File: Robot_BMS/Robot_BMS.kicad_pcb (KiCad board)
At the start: 4 copper layers, 108.6 x 103.7 mm, 117 parts, among them IC1 AP33772DKZ-13, IC1 STUSB4710AQTR, IC2 BQ76922RSNR, J1 632723300011, J2 39-30-0040, J3 Qwiik1, J4 Qwiik1, J5 Qwiik1, J6 Qwiik1, J7 694108301002, J8 691137710002, Q1 2N7002, Q2 NDT3055L, Q3 NDT3055L, Q4 SIS413DN-T1-GE3, Q5 2N7002, Q6 SIS413DN-T1-GE3, U1 TPS54308DDCR, U2 LM3488MM, U3 CSD18563Q5A

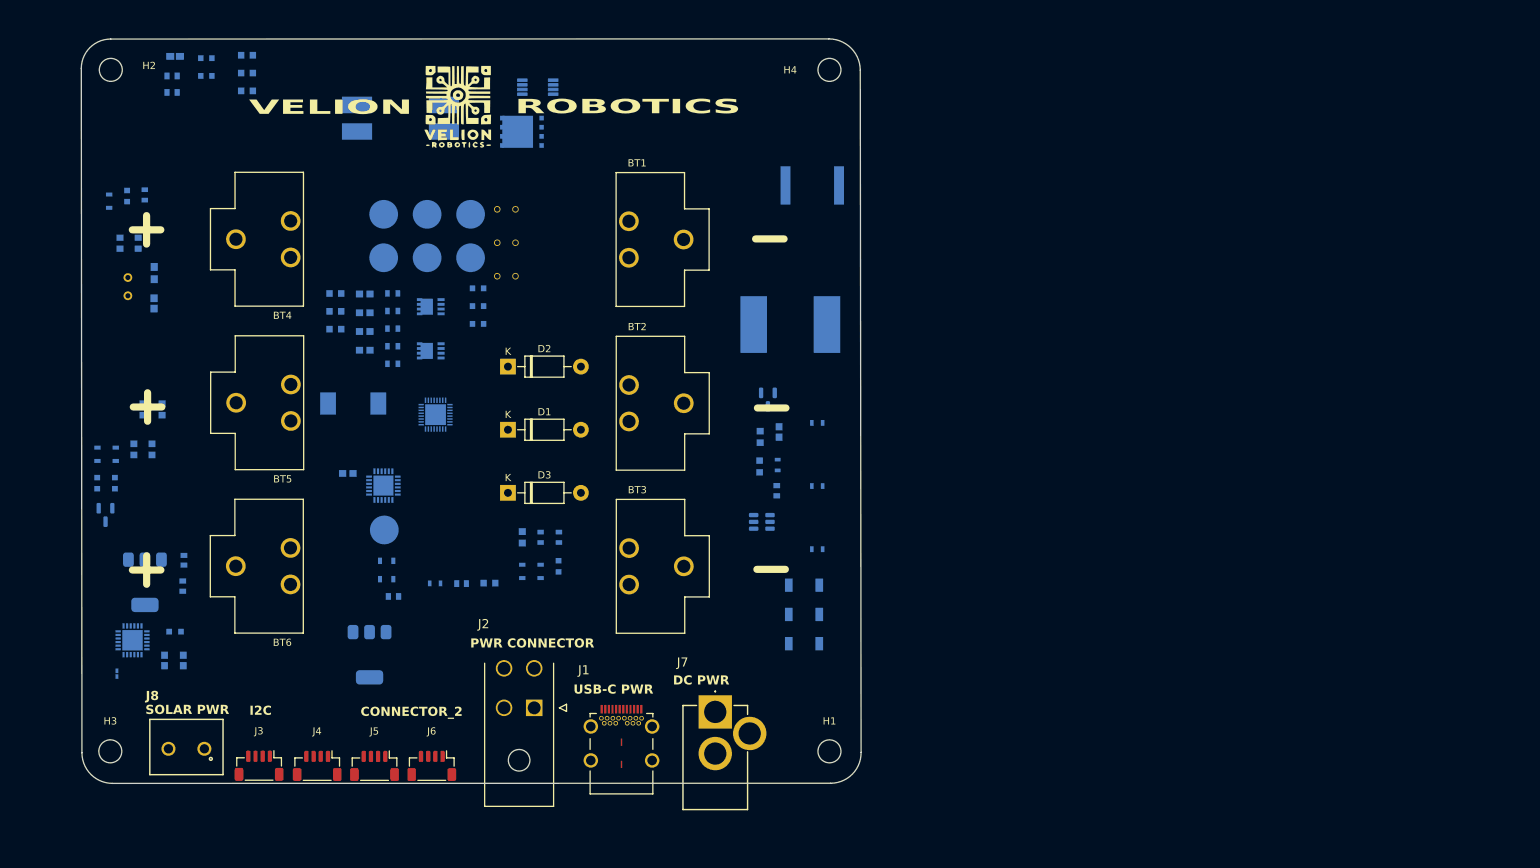
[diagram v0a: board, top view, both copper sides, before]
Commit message: PCB layout up to charging circuit
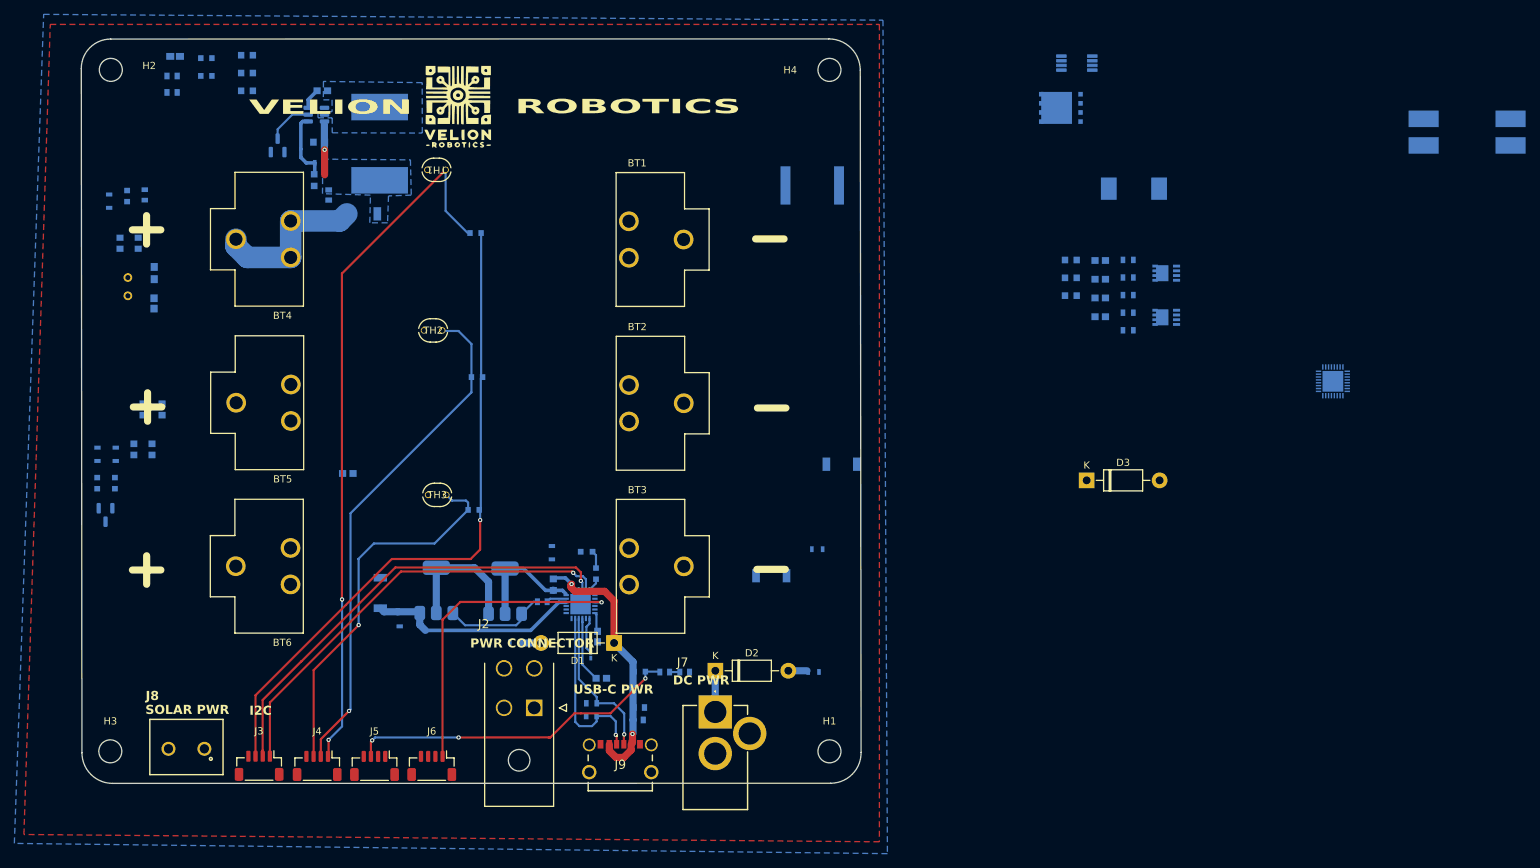
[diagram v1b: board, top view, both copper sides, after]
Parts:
- removed the C4 at (108.8, 91.3)
- removed the C5 at (108.8, 93.9)
- removed the IC1 at (108.4, 80.8)
- removed J1: 632723300011, RobotBMS:632723300011
- removed R12: 100, RobotBMS:RESC1608X55N
- removed the R6 at (115.6, 94.5)
- removed TP1, TP2: NTC1, TestPoint:TestPoint_Pad_D4.0mm
- removed TP3, TP4: NTC2, TestPoint:TestPoint_Pad_D4.0mm
- removed TP5, TP6: NTC3, TestPoint:TestPoint_Pad_D4.0mm
- removed TP7: VBUS_Test, TestPoint:TestPoint_Pad_D4.0mm
- added CR4: CMS05TE12L_Q_M, RobotBMS:M-FLAT_TOS, B.Cu at (105.4, 43.0)
- added J9: UJC-H-G-SMT-P6-TR, RobotBMS:UJCHGSMT2P6TR, F.Cu at (141.3, 119.9)
- added R35: 10k, RobotBMS:RC0603N_YAG, B.Cu at (144.1, 106.8)
- added R36: 1k, RobotBMS:RES_V0603_VIS, B.Cu at (150.3, 106.8)
- TH1, TH2, TH3: moved to F.Cu
- moved L2 148.5 mm to (259.3, 31.6)
- moved IC2 125.0 mm to (240.6, 66.3)
- moved D4 112.8 mm to (212.9, 39.5)
- moved R19 102.5 mm to (204.1, 49.4)
- moved R21 102.5 mm to (204.1, 51.9)
- moved R24 102.5 mm to (204.1, 54.4)
- moved C12 102.5 mm to (208.2, 49.5)
- moved C13 102.5 mm to (208.2, 52.1)
- moved C14 102.5 mm to (208.2, 54.7)
- moved C16 102.5 mm to (208.2, 57.3)
- moved Q4 102.5 mm to (217.3, 51.3)
- moved Q6 102.5 mm to (217.3, 57.4)
- moved R14 102.5 mm to (212.1, 49.4)
- moved R15 102.5 mm to (212.1, 51.9)
- moved R16 102.5 mm to (212.1, 54.3)
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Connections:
- C3 pad 2: BATT+ -> Net-(C3-Pad2)
- J5 pad 3: GND -> /To MCU OR System/MCU_USB_DETECT
- L1 pad 2: BATT+ -> Net-(C3-Pad2)
- R11 pad 1: VBUS -> /To MCU OR System/MCU_USB_DETECT
- R11 pad 2: GND -> Net-(R11-Pad2)
- R4 pad 2: BATT+ -> Net-(C3-Pad2)
- TH1 pad 1: unconnected-(TH1-Pad1) -> /Thermistors/ADC1_MCU
- TH1 pad 2: unconnected-(TH1-Pad2) -> GND
- TH2 pad 1: unconnected-(TH2-Pad1) -> GND
- TH2 pad 2: unconnected-(TH2-Pad2) -> /Thermistors/ADC2_MCU
- TH3 pad 1: unconnected-(TH3-Pad1) -> GND
- TH3 pad 2: unconnected-(TH3-Pad2) -> /Thermistors/ADC3_MCU
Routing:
- net /Thermistors/ADC1_MCU: track 0.00 -> 98.5 mm, vias 0 -> 2
- net 3V3: track 0.00 -> 92.6 mm, vias 0 -> 1
- net /Thermistors/ADC2_MCU: track 0.00 -> 70.9 mm, vias 0 -> 1
- net /Battery Management/SDA: track 0.00 -> 62.6 mm, vias 0 -> 1
- net /Battery Management/SCL: track 0.00 -> 60.9 mm, vias 0 -> 1
- net /Thermistors/ADC3_MCU: track 0.00 -> 52.7 mm, vias 0 -> 1
- net /To MCU OR System/MCU_USB_DETECT: track 0.00 -> 47.1 mm, vias 0 -> 3
- net /To MCU OR System/USB_C_Interrupt: track 0.00 -> 43.2 mm, vias 0 -> 1
- net VBUS: track 0.00 -> 38.3 mm, vias 0 -> 2
- net /Charging Circuit/USB_C: track 0.00 -> 30.2 mm
- net /USB-C/CC1: track 0.00 -> 25.0 mm, vias 0 -> 1
- net BATT+: track 0.00 -> 22.6 mm
- net /USB-C/CC2: track 0.00 -> 21.6 mm, vias 0 -> 1
- net Net-(Q2-S): track 0.00 -> 18.8 mm
- net /USB-C/VCC: track 0.00 -> 16.3 mm
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- added copper zone on B.Cu, net GND
- added copper zone on F.Cu, net GND
- added copper zone on B.Cu, net Net-(C3-Pad2)
- added copper zone on B.Cu, net Net-(U1-SW)
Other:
- copper layers 4 -> 2
- board text removed: "CONNECTOR_2"

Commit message: halfway throgh battery management pcb layout
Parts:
- NTC1: renamed from RT1; value 10k -> 10000
- moved C20 170.6 mm to (246.0, 73.9)
- moved C22 170.6 mm to (242.4, 71.6)
- moved C25 170.6 mm to (239.8, 59.7)
- moved R30 170.6 mm to (241.3, 65.5)
- moved R33 170.6 mm to (243.8, 65.5)
- moved R35 170.6 mm to (242.3, 59.0)
- moved C23 170.6 mm to (246.1, 69.7)
- moved R29 170.6 mm to (244.7, 58.8)
- moved C21 144.6 mm to (243.8, 113.9)
- moved C24 123.3 mm to (193.4, 68.1)
- moved C26 123.3 mm to (193.0, 70.8)
- moved C27 123.3 mm to (193.0, 73.1)
- moved R31 123.3 mm to (203.4, 67.9)
- moved R32 123.3 mm to (203.4, 70.4)
- moved R34 123.3 mm to (203.4, 72.9)
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- renumbered CR4 to CR1, CR1 to CR2, CR2 to CR3, CR3 to CR4, J9 to J1, J2 to J3, J3 to J4, J4 to J5, J5 to J6, J6 to J7, J7 to J8, J8 to J9, R35 to R11, R11 to R12, R36 to R13, R13 to R14, R14 to R15, R15 to R16, R16 to R17, R17 to R18, R18 to R19, R19 to R20, R20 to R21, R21 to R22, R22 to R23, R23 to R24, R24 to R25, R25 to R26, R26 to R27, R27 to R28, R28 to R29, R29 to R30, R30 to R31, R31 to R32, R32 to R33, R33 to R34, R34 to R35
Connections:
- CR1 pad 2: BATT+ -> /Charging Circuit/TO_LOAD
- J3 pad 1: GND -> /Battery Management/TO_LOAD_GND
- J3 pad 2: GND -> /Battery Management/TO_LOAD_GND
- Q4 pad 10: (no net) -> BATT+
- Q4 pad 11: (no net) -> BATT+
- Q4 pad 9: (no net) -> BATT+
- Q6 pad 10: (no net) -> Net-(Q4-S_1)
- Q6 pad 11: (no net) -> Net-(Q4-S_1)
- Q6 pad 9: (no net) -> Net-(Q4-S_1)
- R21 pad 1: GND -> /Battery Management/TO_LOAD_GND
- R22 pad 1: GND -> /Battery Management/TO_LOAD_GND
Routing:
- net Net-(BT1-Pad1_1): track 0.00 -> 116.3 mm
- net /Charging Circuit/MCU_CHARGE_EN: track 0.00 -> 111.6 mm, vias 0 -> 1
- net /Battery Management/TO_LOAD: track 0.00 -> 106.5 mm, vias 0 -> 1
- net Net-(BT2-Pad1_1): track 0.00 -> 94.6 mm, vias 0 -> 1
- net /Battery Management/ALERT: track 0.00 -> 57.8 mm, vias 0 -> 1
- net /Battery Management/TO_LOAD_GND: track 0.00 -> 56.1 mm, vias 0 -> 2
- net BATT+: track 22.6 -> 71.9 mm, vias 0 -> 2
- net 3V3: track 92.6 -> 58.5 mm
- net /Thermistors/ADC2_MCU: track 70.9 -> 99.0 mm
- net /Thermistors/ADC1_MCU: track 98.5 -> 70.9 mm, vias 2 -> 4
- net /Battery Management/SCL: track 60.9 -> 85.8 mm, vias 1 -> 4
- net /Battery Management/SDA: track 62.6 -> 87.2 mm, vias 1 -> 2
- net Net-(Q6-S_1): track 0.00 -> 21.5 mm
- net /Battery Management/LD: track 0.00 -> 21.0 mm, vias 0 -> 2
- net Net-(IC2-DSG): track 0.00 -> 19.2 mm, vias 0 -> 2
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
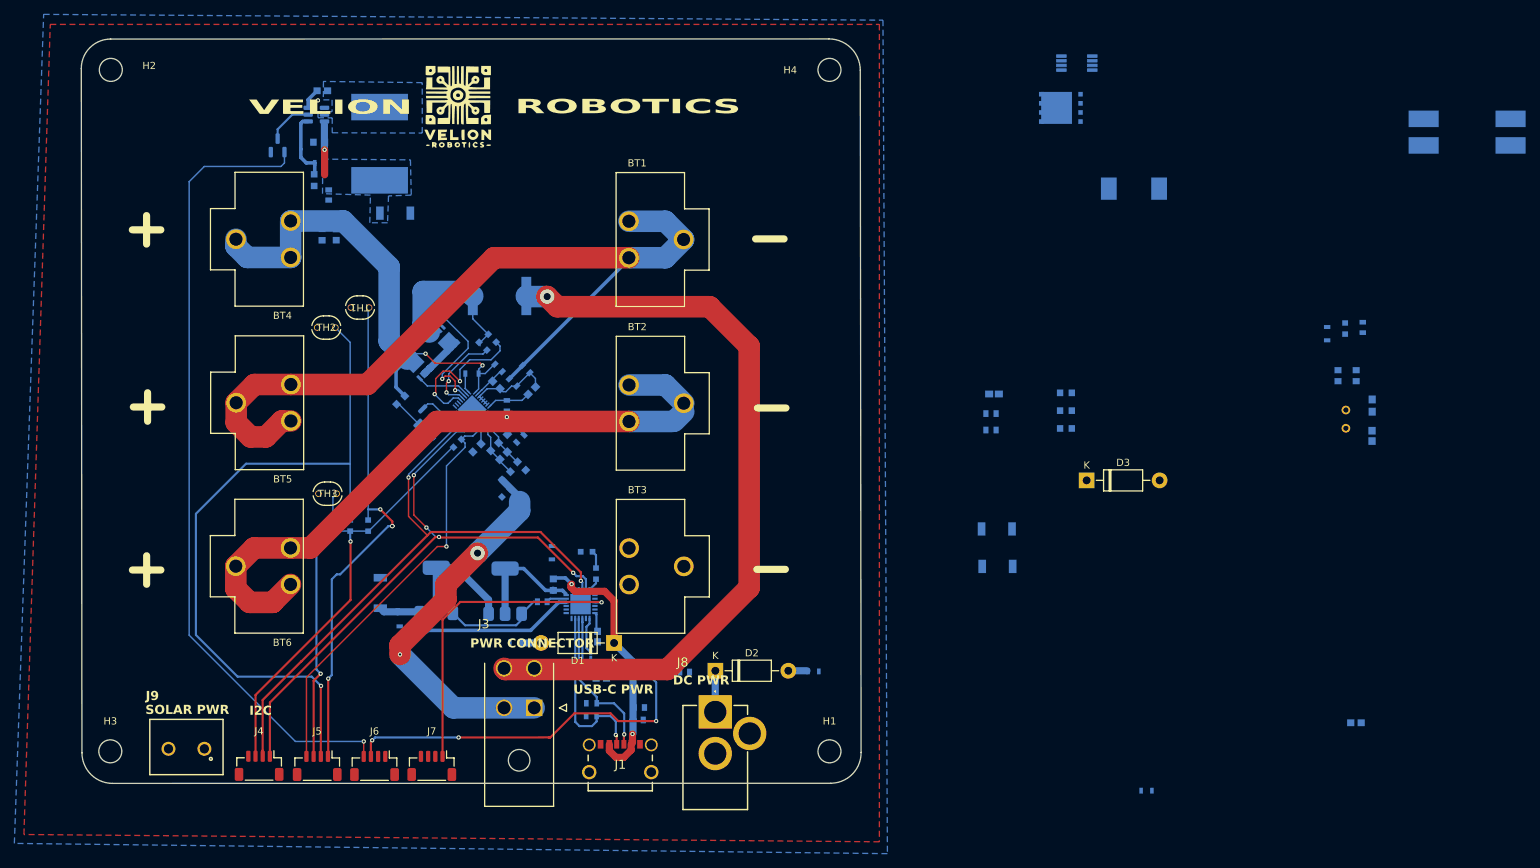
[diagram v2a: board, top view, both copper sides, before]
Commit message: first pcb layout done, beginning of DRC checks
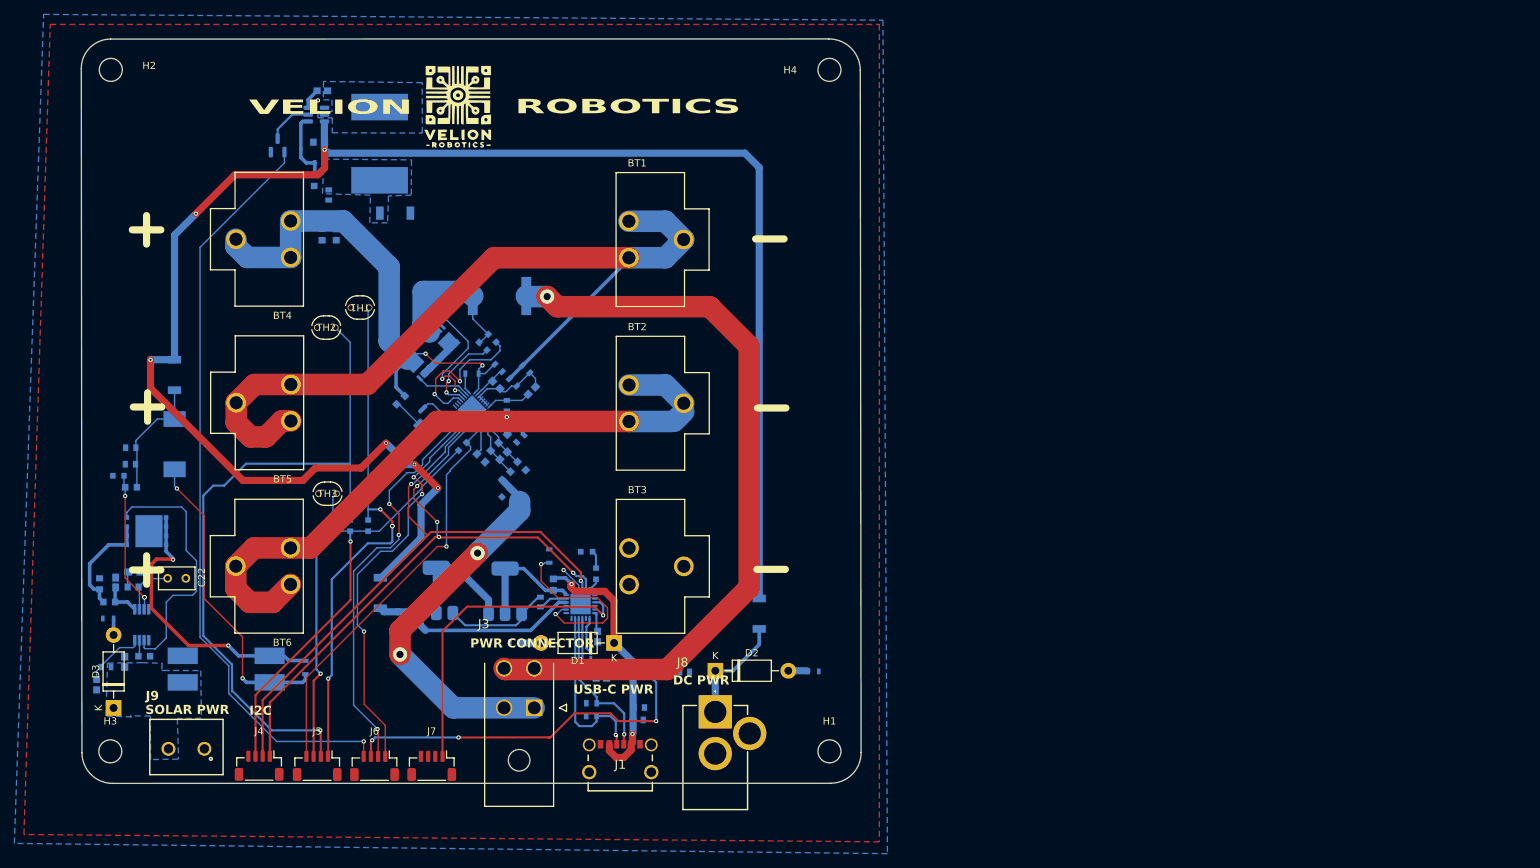
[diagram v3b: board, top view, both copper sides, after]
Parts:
- C22: moved to F.Cu
- moved L2 188.3 mm to (86.5, 106.4)
- moved R29 181.3 mm to (69.7, 106.1), turned to 0 degrees
- moved R33 177.4 mm to (68.8, 94.5)
- moved C20 176.5 mm to (72.3, 105.4)
- moved C21 175.4 mm to (68.4, 108.6), turned to -90 degrees
- moved C23 173.9 mm to (73.7, 92.9), turned to 0 degrees
- moved R35 172.0 mm to (71.5, 79.5), turned to 0 degrees
- moved R30 170.3 mm to (73.5, 95.0), turned to 0 degrees
- moved C22 164.3 mm to (79.6, 93.8), turned to 180 degrees
- moved U2 151.9 mm to (74.7, 100.2), turned to -90 degrees
- moved C25 149.7 mm to (97.5, 106.2)
- moved R28 146.6 mm to (70.0, 99.3), turned to 0 degrees
- moved U3 140.3 mm to (75.4, 87.2), turned to 0 degrees
- moved D3 139.1 mm to (70.8, 111.8), turned to 90 degrees
- moved D4 138.2 mm to (79.3, 75.1), turned to -90 degrees
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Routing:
- net /Charging Circuit/CHARGE_IN: track 7.13 -> 243.1 mm, vias 1 -> 6
- net /Battery Management/MCU_DISCHRG_CTRL: track 0.00 -> 57.5 mm, vias 0 -> 3
- net /Battery Management/MCU_CHRG_CTRL: track 0.00 -> 56.4 mm, vias 0 -> 3
- net Net-(D4-A): track 0.00 -> 43.0 mm, vias 0 -> 2
- net Net-(C25-Pad1): track 0.00 -> 40.1 mm, vias 0 -> 2
- net Net-(U2-DR): track 0.00 -> 35.9 mm
- net Net-(IC1-V5V): track 0.00 -> 25.6 mm, vias 0 -> 2
- net Net-(U2-FB): track 0.00 -> 19.8 mm, vias 0 -> 3
- net /Charging Circuit/SOLAR_15V_OUT: track 0.00 -> 17.3 mm
- net /Solar Power/DR_Source: track 0.00 -> 15.4 mm
- net GND: track 0.09 -> 12.2 mm, vias 1 -> 2
- net /Charging Circuit/DC_BARREL_JACK: track 5.74 -> 15.5 mm
- net Net-(U2-VIN): track 0.00 -> 8.79 mm
- net Net-(U2-COMP): track 0.00 -> 8.26 mm
- net /Charging Circuit/MCU_CHARGE_EN: track 111.6 -> 105.6 mm
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- added copper zone on B.Cu, net /Solar Power/SOLAR_VIN

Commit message: resize board for chanin m2.5 holes
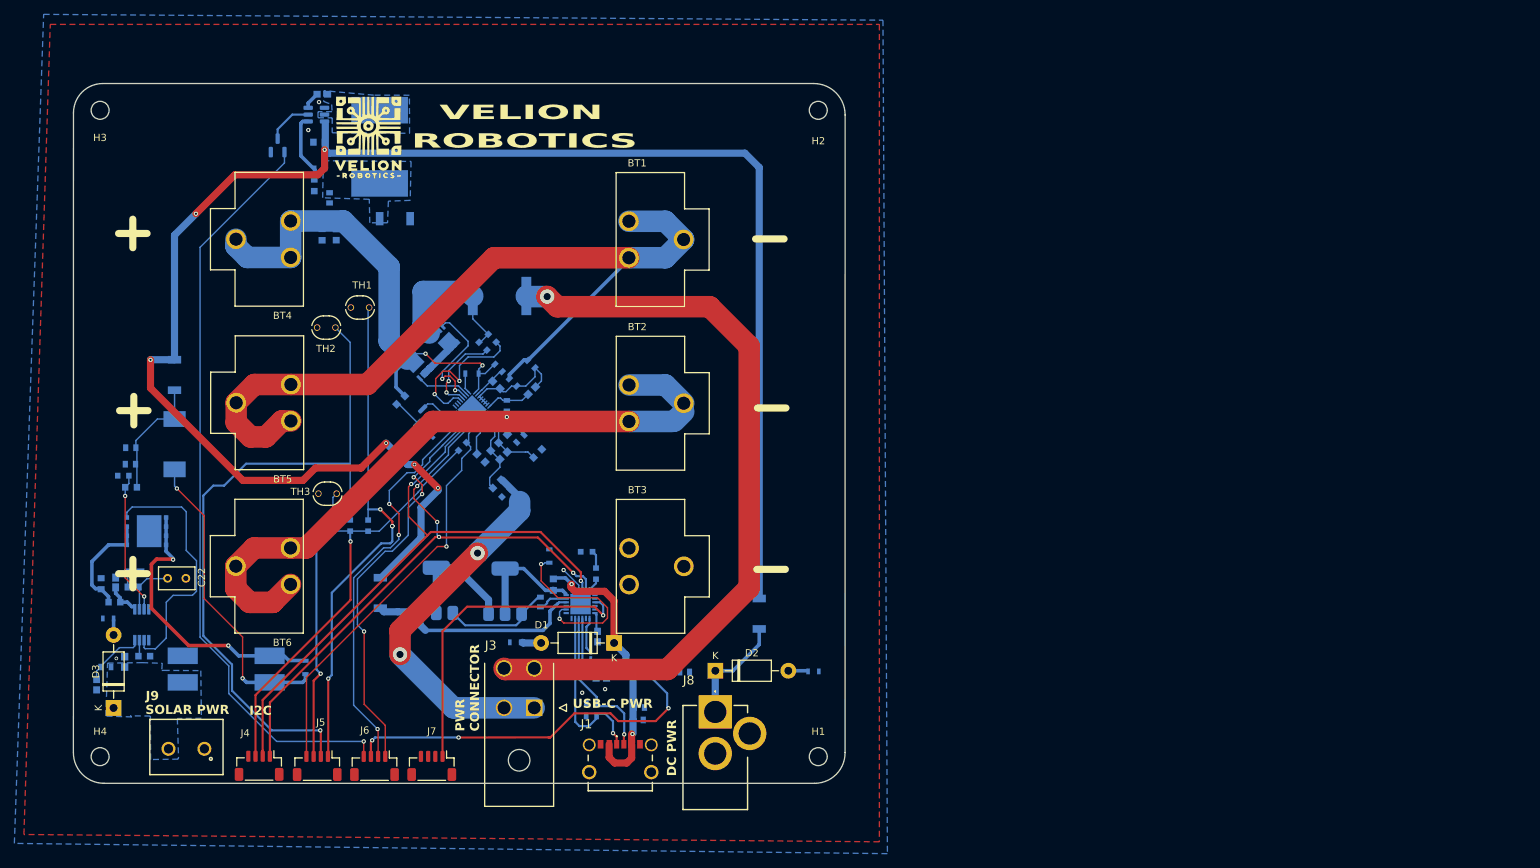
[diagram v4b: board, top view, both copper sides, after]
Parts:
- H1, H2, H3, H4: footprint MountingHole:MountingHole_3.2mm_M3 -> MountingHole:MountingHole_2.5mm
- moved H4 139.5 mm to (68.9, 118.6)
- moved H2 98.7 mm to (168.9, 28.6)
- moved H3 89.3 mm to (68.9, 28.6)
- moved ? 13.2 mm to (110.9, 36.3)
- moved R20 2.84 mm to (129.8, 76.4), turned to -135 degrees
- moved H1 1.73 mm to (168.9, 118.6)
- moved R22 1.72 mm to (124.2, 80.6), turned to -135 degrees
- moved R16 1.00 mm to (129.0, 63.9)
- moved R4 0.78 mm to (99.5, 36.7)
- moved CR1 0.77 mm to (110.0, 43.7)
- moved R32 0.72 mm to (70.9, 97.1)
- moved R5 0.72 mm to (98.7, 39.0)
- moved R35 0.68 mm to (72.2, 79.5)
- moved C2 0.48 mm to (99.9, 26.4)
- moved L1 0.43 mm to (107.8, 33.7)
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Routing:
- net Net-(IC2-SRN): track 8.96 -> 11.9 mm
- net Net-(IC2-VC2): track 12.7 -> 15.6 mm
- net Net-(IC2-DSG): track 19.2 -> 16.9 mm
- net Net-(IC2-SRP): track 8.16 -> 10.2 mm
- net VBUS: track 38.3 -> 40.2 mm
- net /To MCU OR System/MCU_USB_DETECT: track 53.6 -> 55.0 mm
- net /Thermistors/ADC1_MCU: track 72.1 -> 71.0 mm
- net /Charging Circuit/USB_C: track 30.2 -> 31.2 mm
- net /Solar Power/Isense: track 5.23 -> 4.30 mm
- net Net-(IC1-V5V): track 25.6 -> 25.0 mm
- net /Battery Management/MCU_DISCHRG_CTRL: track 57.5 -> 57.0 mm
- net Net-(U2-FB): track 19.8 -> 20.2 mm, vias 3 -> 2
- net GND: vias 2 -> 6
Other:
- board size 108.6 x 103.7 mm -> 107.5 x 97.4 mm
- board text added: "In Centre"
- board text added: "K"

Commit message: manufacture ready
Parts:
- moved C18 1.36 mm to (120.7, 77.4), turned to 45 degrees
- moved C4 0.32 mm to (144.3, 111.8)
- moved C9 0.28 mm to (144.1, 113.5)
- moved R11 0.26 mm to (144.3, 106.9)
- moved R27 0.17 mm to (168.4, 106.7)
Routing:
- net /Battery Management/SDA: track 86.7 -> 88.0 mm
- net Net-(IC2-SRN): track 11.9 -> 12.5 mm
- net /Charging Circuit/CHARGE_IN: track 243.1 -> 243.6 mm
